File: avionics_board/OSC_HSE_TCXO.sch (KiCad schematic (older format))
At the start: 5 parts, among them X2 ECS-TXO-2016

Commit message: Removed unecessary footprint lib
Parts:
- X2: footprint avionics_board:Oscillator_SMD_ECS_TXO-2016-xx-xxx-4Pin_2.0x1.6mm -> footprint_custom:Oscillator_SMD_ECS_TXO-2016-xx-xxx-4Pin_2.0x1.6mm
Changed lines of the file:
@@
 F 0 "X2" H 5225 4100 50  0000 R CNN
 F 1 "ECS-TXO-2016" H 5225 3525 50  0000 R CNN
-F 2 "avionics_board:Oscillator_SMD_ECS_TXO-2016-xx-xxx-4Pin_2.0x1.6mm" H 5225 2900 50  0001 C CNN
+F 2 "footprint_custom:Oscillator_SMD_ECS_TXO-2016-xx-xxx-4Pin_2.0x1.6mm" H 5225 2900 50  0001 C CNN
 F 3 "https://ecsxtal.com/store/pdf/ECS-TXO-2016.pdf" H 5250 3925 50  0001 C CNN
 F 4 "ECS-TXO-2016-33-100-TR" H 5425 3000 50  0001 C CNN "Mfr. #"

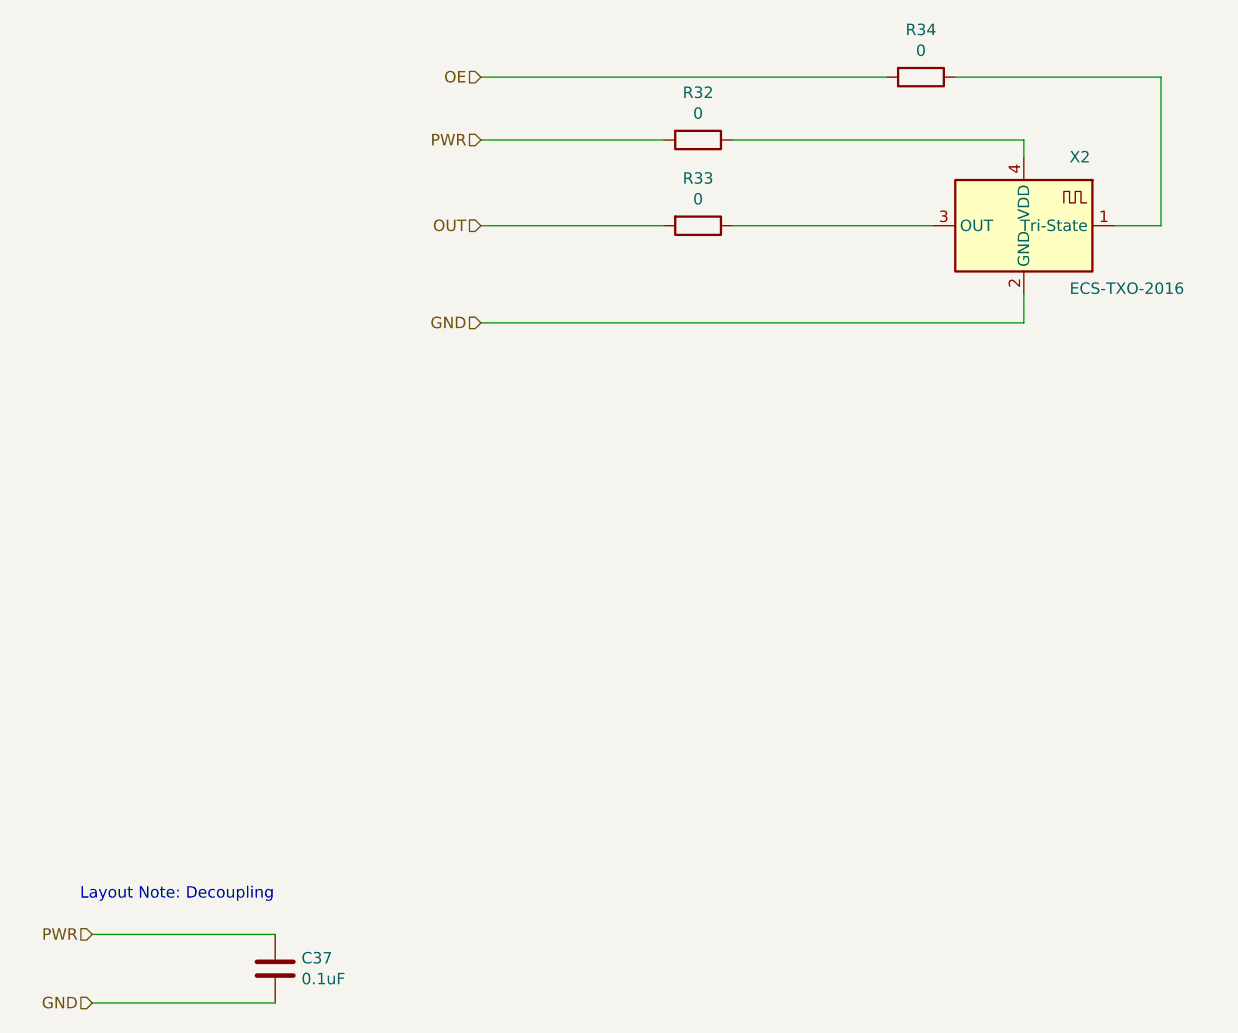
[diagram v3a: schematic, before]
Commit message: Update Avionics part names to match KiCad update. Update Avionics board to use new interboard connector
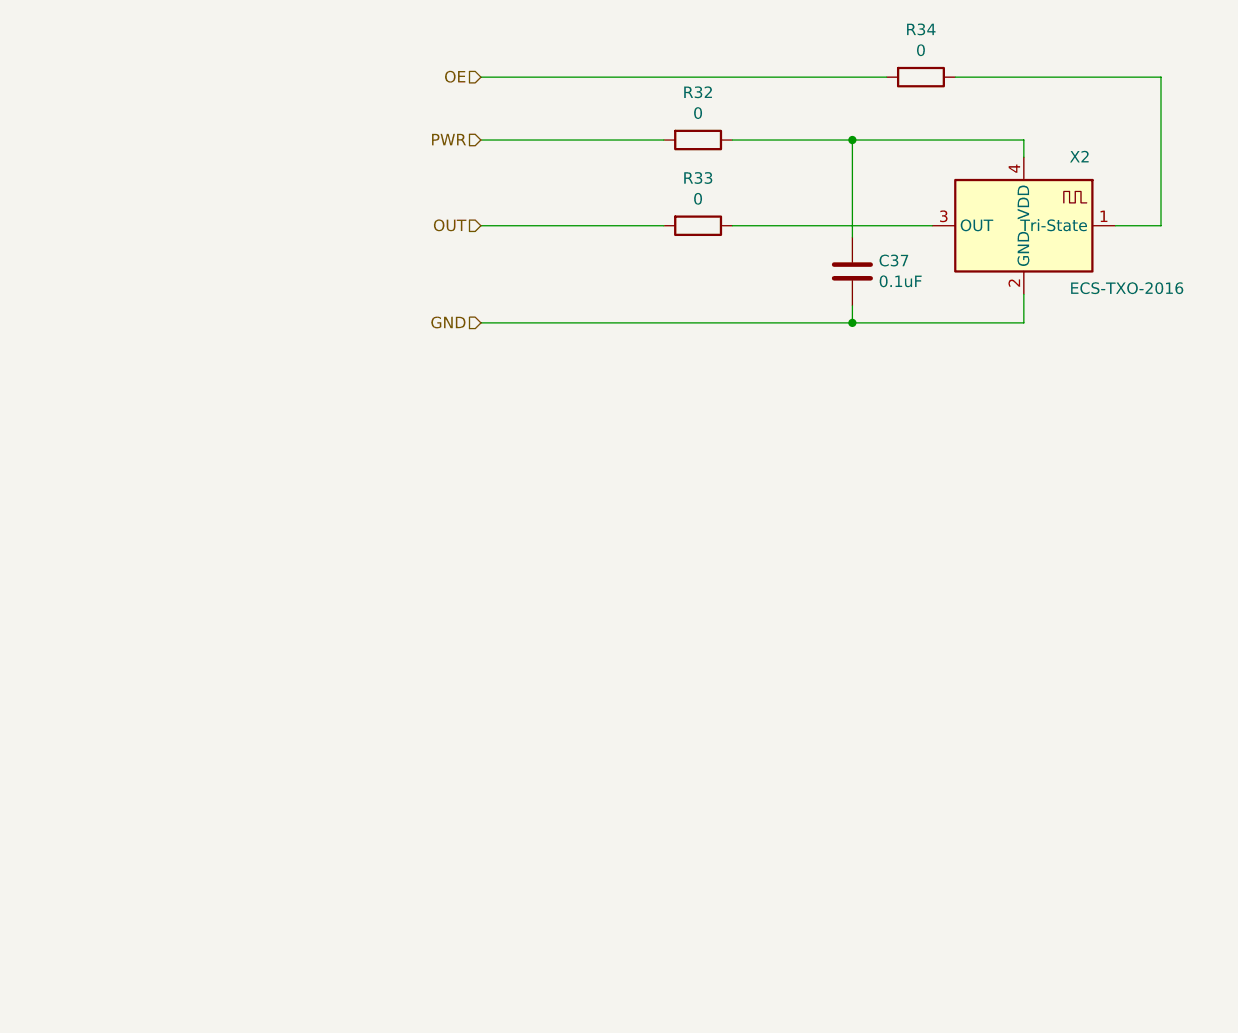
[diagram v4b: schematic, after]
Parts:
- C37: footprint Capacitor_SMD:C_0603_1608Metric_Pad1.05x0.95mm_HandSolder -> Capacitor_SMD:C_0603_1608Metric_Pad1.08x0.95mm_HandSolder
- R32, R33, R34: footprint Resistor_SMD:R_0603_1608Metric_Pad1.05x0.95mm_HandSolder -> Resistor_SMD:R_0603_1608Metric_Pad0.98x0.95mm_HandSolder
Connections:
- net PWR: no longer C37.1
- net at R32.1, X2.4 (VDD): now also C37.1
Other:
- note removed: "Layout Note: Decoupling\n"
- moved on the sheet: C37
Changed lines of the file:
@@
 $Descr A 11000 8500
 encoding utf-8
-Sheet 11 23
+Sheet 10 23
 Title "10MHz TCXO"
 Date "2020-05-25"
@@
 	-1   0    0    -1
 $EndComp
-Text Notes 2145 6755 2    50   ~ 0
-Layout Note: Decoupling\n
-Text HLabel 1350 6900 0    50   Input ~ 0
-PWR
-Text HLabel 1350 7200 0    50   Input ~ 0
-GND
 $Comp
 L Device:C C?
 U 1 1 600759A7
-P 2150 7050
+P 4675 4000
 AR Path="/5EA31C93/5EA7CBB1/600759A7" Ref="C?"  Part="1"
 AR Path="/5EA31C93/5EAB027D/600759A7" Ref="C?"  Part="1"
@@
 AR Path="/5EA31C93/5FEDB823/600759A7" Ref="C?"  Part="1"
 AR Path="/5EA31C93/600564FD/600759A7" Ref="C37"  Part="1"
-F 0 "C37" H 2265 7096 50  0000 L CNN
-F 1 "0.1uF" H 2265 7005 50  0000 L CNN
-F 2 "Capacitor_SMD:C_0603_1608Metric_Pad1.05x0.95mm_HandSolder" H 2188 6900 50  0001 C CNN
-F 3 "~" H 2150 7050 50  0001 C CNN
-F 4 "25V" H 2150 7050 50  0001 C CNN "Voltage"
-F 5 "CL10B104KA8NNNC" H 2150 7050 50  0001 C CNN "Mfr. #"
-F 6 "https://www.digikey.com/product-detail/en/samsung-electro-mechanics/CL10B104KA8NNNC/1276-1006-1-ND/3889092" H 2150 7050 50  0001 C CNN "Order"
-	1    2150 7050
+F 0 "C37" H 4790 4046 50  0000 L CNN
+F 1 "0.1uF" H 4790 3955 50  0000 L CNN
+F 2 "Capacitor_SMD:C_0603_1608Metric_Pad1.08x0.95mm_HandSolder" H 4713 3850 50  0001 C CNN
+F 3 "~" H 4675 4000 50  0001 C CNN
+F 4 "25V" H 4675 4000 50  0001 C CNN "Voltage"
+F 5 "CL10B104KA8NNNC" H 4675 4000 50  0001 C CNN "Mfr. #"
+F 6 "https://www.digikey.com/product-detail/en/samsung-electro-mechanics/CL10B104KA8NNNC/1276-1006-1-ND/3889092" H 4675 4000 50  0001 C CNN "Order"
+	1    4675 4000
 	1    0    0    -1
 $EndComp
-Wire Wire Line
-	1350 6900 2150 6900
-Wire Wire Line
-	1350 7200 2150 7200
 $Comp
 L Device:R R?
@@
 F 0 "R32" V 3793 3425 50  0000 C CNN
 F 1 "0" V 3884 3425 50  0000 C CNN
-F 2 "Resistor_SMD:R_0603_1608Metric_Pad1.05x0.95mm_HandSolder" V 3930 3425 50  0001 C CNN
+F 2 "Resistor_SMD:R_0603_1608Metric_Pad0.98x0.95mm_HandSolder" V 3930 3425 50  0001 C CNN
 F 3 "~" H 4000 3425 50  0001 C CNN
 F 4 "RK73Z1JTTD" H 4000 3425 50  0001 C CNN "Mfr. #"
@@
 F 0 "R34" V 4768 3150 50  0000 C CNN
 F 1 "0" V 4859 3150 50  0000 C CNN
-F 2 "Resistor_SMD:R_0603_1608Metric_Pad1.05x0.95mm_HandSolder" V 4905 3150 50  0001 C CNN
+F 2 "Resistor_SMD:R_0603_1608Metric_Pad0.98x0.95mm_HandSolder" V 4905 3150 50  0001 C CNN
 F 3 "~" H 4975 3150 50  0001 C CNN
 F 4 "RK73Z1JTTD" H 4975 3150 50  0001 C CNN "Mfr. #"
@@
 F 0 "R33" V 3793 3800 50  0000 C CNN
 F 1 "0" V 3884 3800 50  0000 C CNN
-F 2 "Resistor_SMD:R_0603_1608Metric_Pad1.05x0.95mm_HandSolder" V 3930 3800 50  0001 C CNN
+F 2 "Resistor_SMD:R_0603_1608Metric_Pad0.98x0.95mm_HandSolder" V 3930 3800 50  0001 C CNN
 F 3 "~" H 4000 3800 50  0001 C CNN
 F 4 "RK73Z1JTTD" H 4000 3800 50  0001 C CNN "Mfr. #"
@@
 	3050 3800 3850 3800
 Wire Wire Line
-	3050 4225 5425 4225
+	3050 4225 4675 4225
 Wire Wire Line
 	3050 3425 3850 3425
@@
 	5425 3425 5425 3500
 Wire Wire Line
-	4150 3425 5425 3425
+	4150 3425 4675 3425
 Wire Wire Line
 	4150 3800 5025 3800
@@
 Wire Wire Line
 	5125 3150 6025 3150
+Wire Wire Line
+	4675 3850 4675 3425
+Connection ~ 4675 3425
+Wire Wire Line
+	4675 3425 5425 3425
+Wire Wire Line
+	4675 4150 4675 4225
+Connection ~ 4675 4225
+Wire Wire Line
+	4675 4225 5425 4225
 $EndSCHEMATC
